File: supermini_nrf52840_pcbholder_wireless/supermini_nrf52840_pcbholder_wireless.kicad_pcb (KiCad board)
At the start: 2 copper layers, 117.8 x 38.4 mm, 18 parts, among them J10 Conn_01x08_Pin, J11 Conn_01x08_Pin, J12 Conn_01x08_Pin, J5 Conn_01x02_Pin, J6 Conn_01x02_Pin, J7 Conn_01x04_Pin, J8 Conn_01x04_Pin, J9 Conn_01x08_Pin, SW1 SW_SPDT, SW2 SW_SPST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

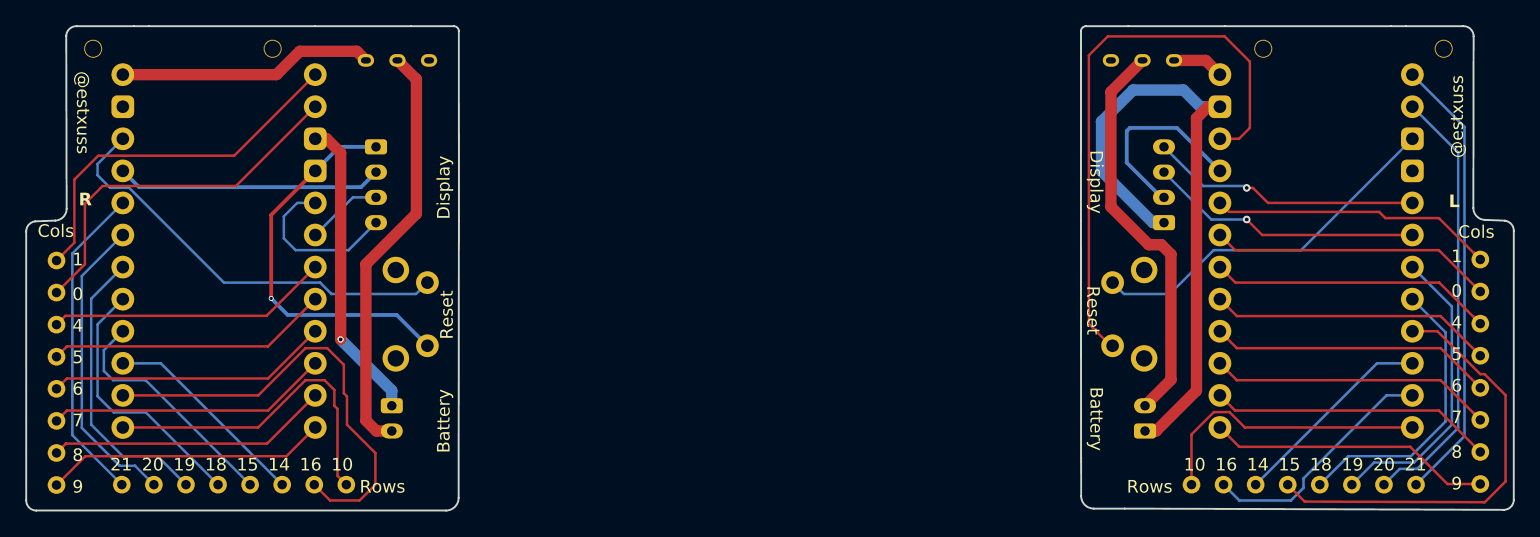
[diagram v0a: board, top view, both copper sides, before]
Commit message: change power switch footprint and supermini board placement
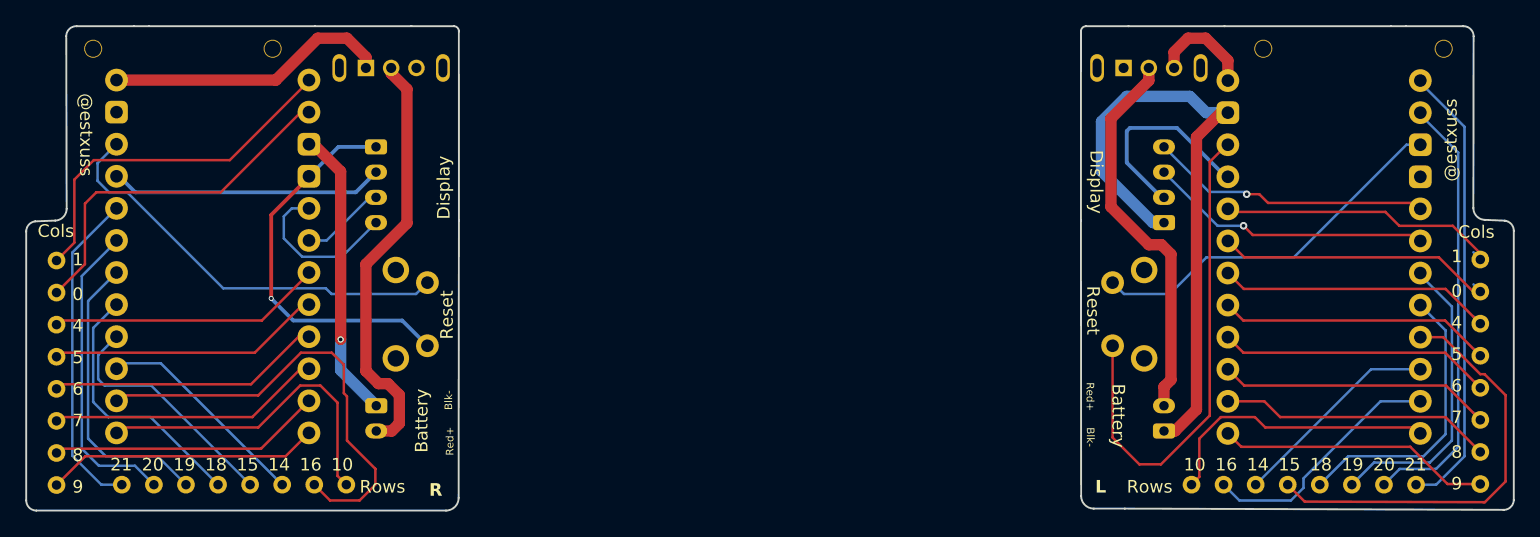
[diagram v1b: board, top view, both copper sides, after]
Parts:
- removed ? (x4): , #footprint:M1.4_tapping_Hole_rev2
- added H1: MountingHole, #footprint:M1.4_tapping_Hole_rev2, F.Cu at (90.0, 74.8)
- added H2: MountingHole, #footprint:M1.4_tapping_Hole_rev2, F.Cu at (104.2, 74.8)
- added H3: MountingHole, #footprint:M1.4_tapping_Hole_rev2, F.Cu at (182.7, 74.8)
- added H4: MountingHole, #footprint:M1.4_tapping_Hole_rev2, F.Cu at (197.0, 74.8)
- SW1, SW3: footprint #footprint:TGSW_MSK-12D19 -> SLW_864574_5A_RA_N_D:SW_SLW-864574-5A-RA-N-D
- moved SW1 1.72 mm to (113.6, 76.3), turned to 0 degrees
- moved SW3 1.72 mm to (173.6, 76.3), turned to 0 degrees
- moved J5 1.50 mm to (174.8, 105.1)
- moved J6 1.23 mm to (112.4, 103.1)
- moved U5 0.79 mm to (187.5, 91.3)
- moved U6 0.66 mm to (99.5, 91.2)
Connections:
- SW1 pad 1: unconnected-(SW1-A-Pad1) -> R_BAT_POS
- SW1 pad 3: R_BAT_POS -> unconnected-(SW1-C-Pad3)
- SW3 pad 1: L_BAT_POS -> unconnected-(SW3-A-Pad1)
- SW3 pad 3: unconnected-(SW3-C-Pad3) -> L_BAT_POS
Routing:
- net L_RST: track 46.0 -> 39.6 mm
- net L_BAT_POS: track 4.10 -> 8.29 mm
- net R_BAT_POS: track 20.3 -> 22.6 mm
- net R_BAT_NEG: track 24.2 -> 23.1 mm
- net L_SW_POS: track 31.8 -> 30.8 mm
- net L_ROW4: track 23.2 -> 22.4 mm
- net L_ROW8: track 22.5 -> 21.7 mm
- net L_ROW6: track 23.3 -> 22.4 mm
- net L_ROW5: track 23.2 -> 22.4 mm
- net L_ROW3: track 23.2 -> 22.4 mm
- net L_ROW7: track 22.5 -> 21.7 mm
- net L_ROW2: track 23.2 -> 22.4 mm
- net L_OLED_SDA: track 21.5 -> 22.3 mm
- net L_OLED_SCL: track 21.7 -> 22.6 mm
- net L_COL5: track 34.8 -> 34.0 mm
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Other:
- board text added: "Blk-"
- board text added: "Red+"
- board text removed: "SW1"
- board text removed: "SW3"
